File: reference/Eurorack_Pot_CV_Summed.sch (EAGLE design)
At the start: 10 parts, among them J1 Eurorack Jack, U1 MCP6004, U2 LM4040-10V

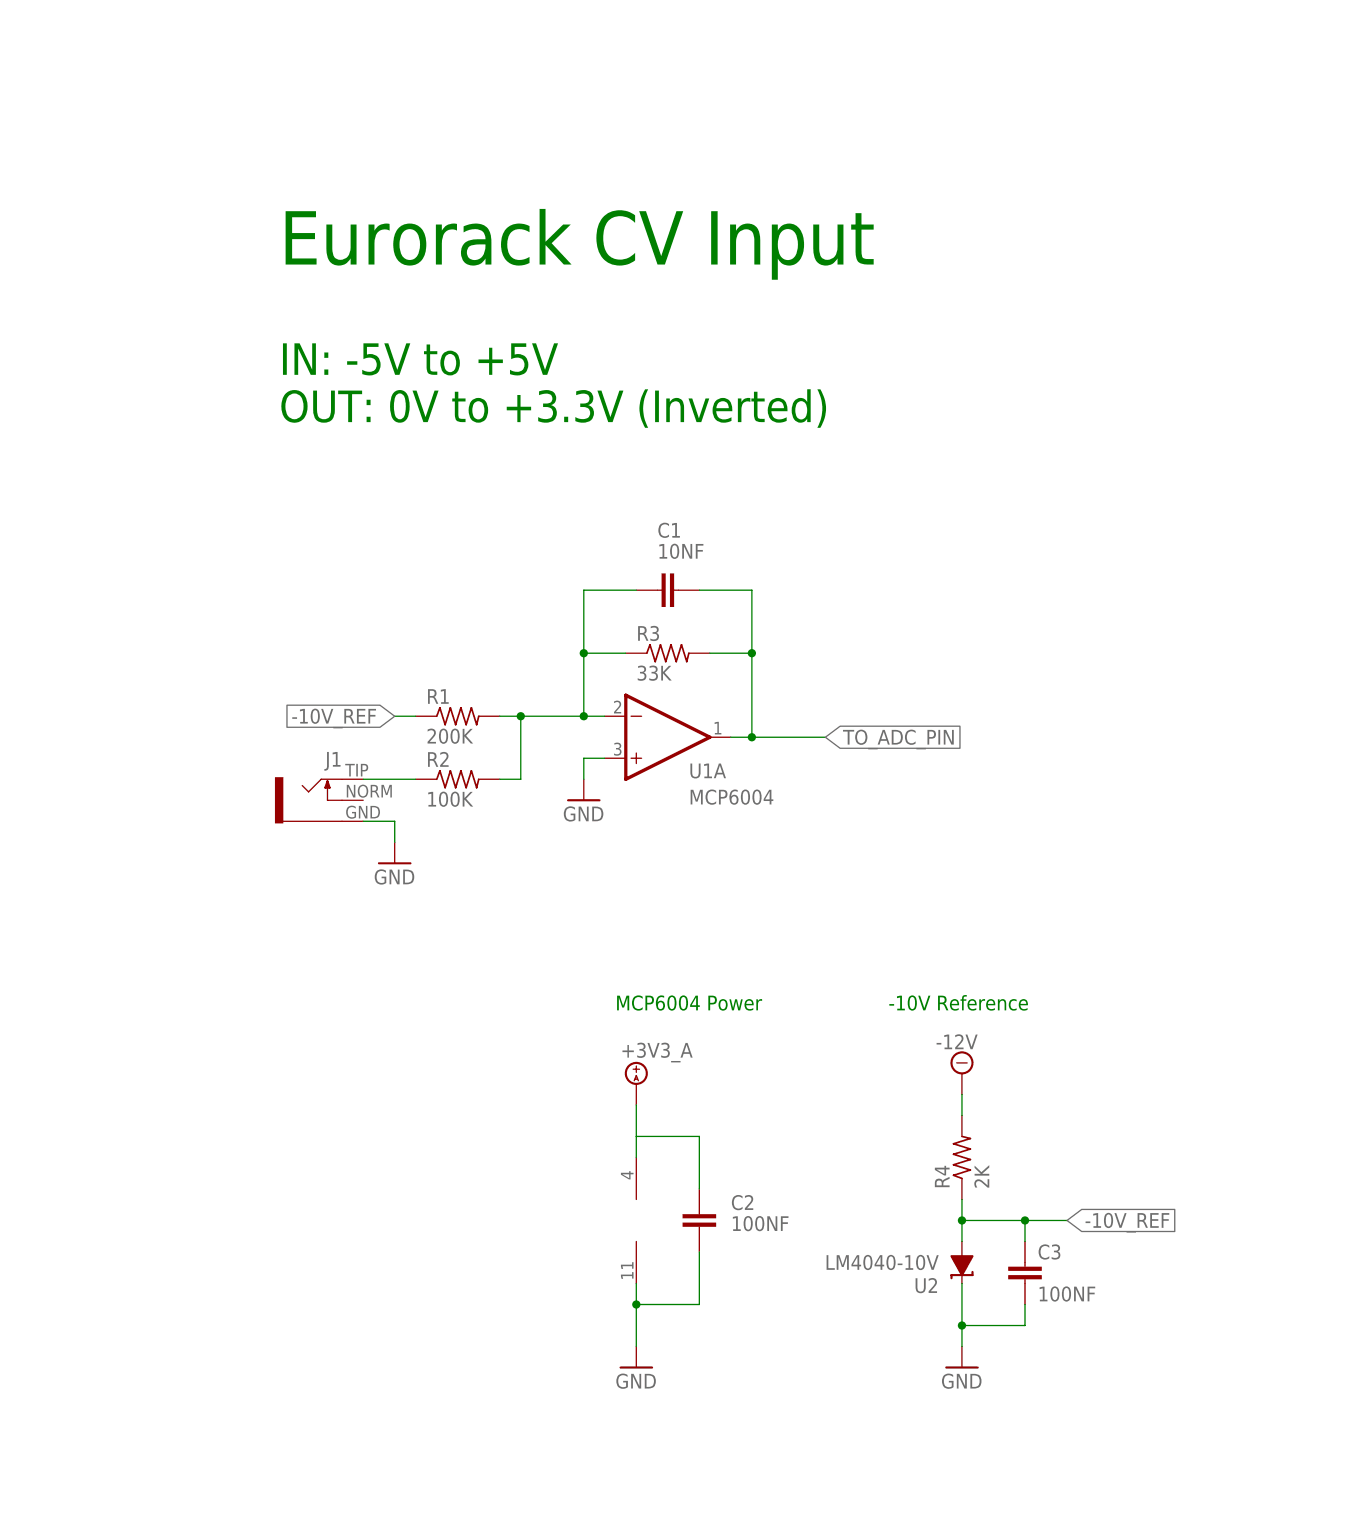
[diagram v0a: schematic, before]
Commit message: added pot in and pot cv summed
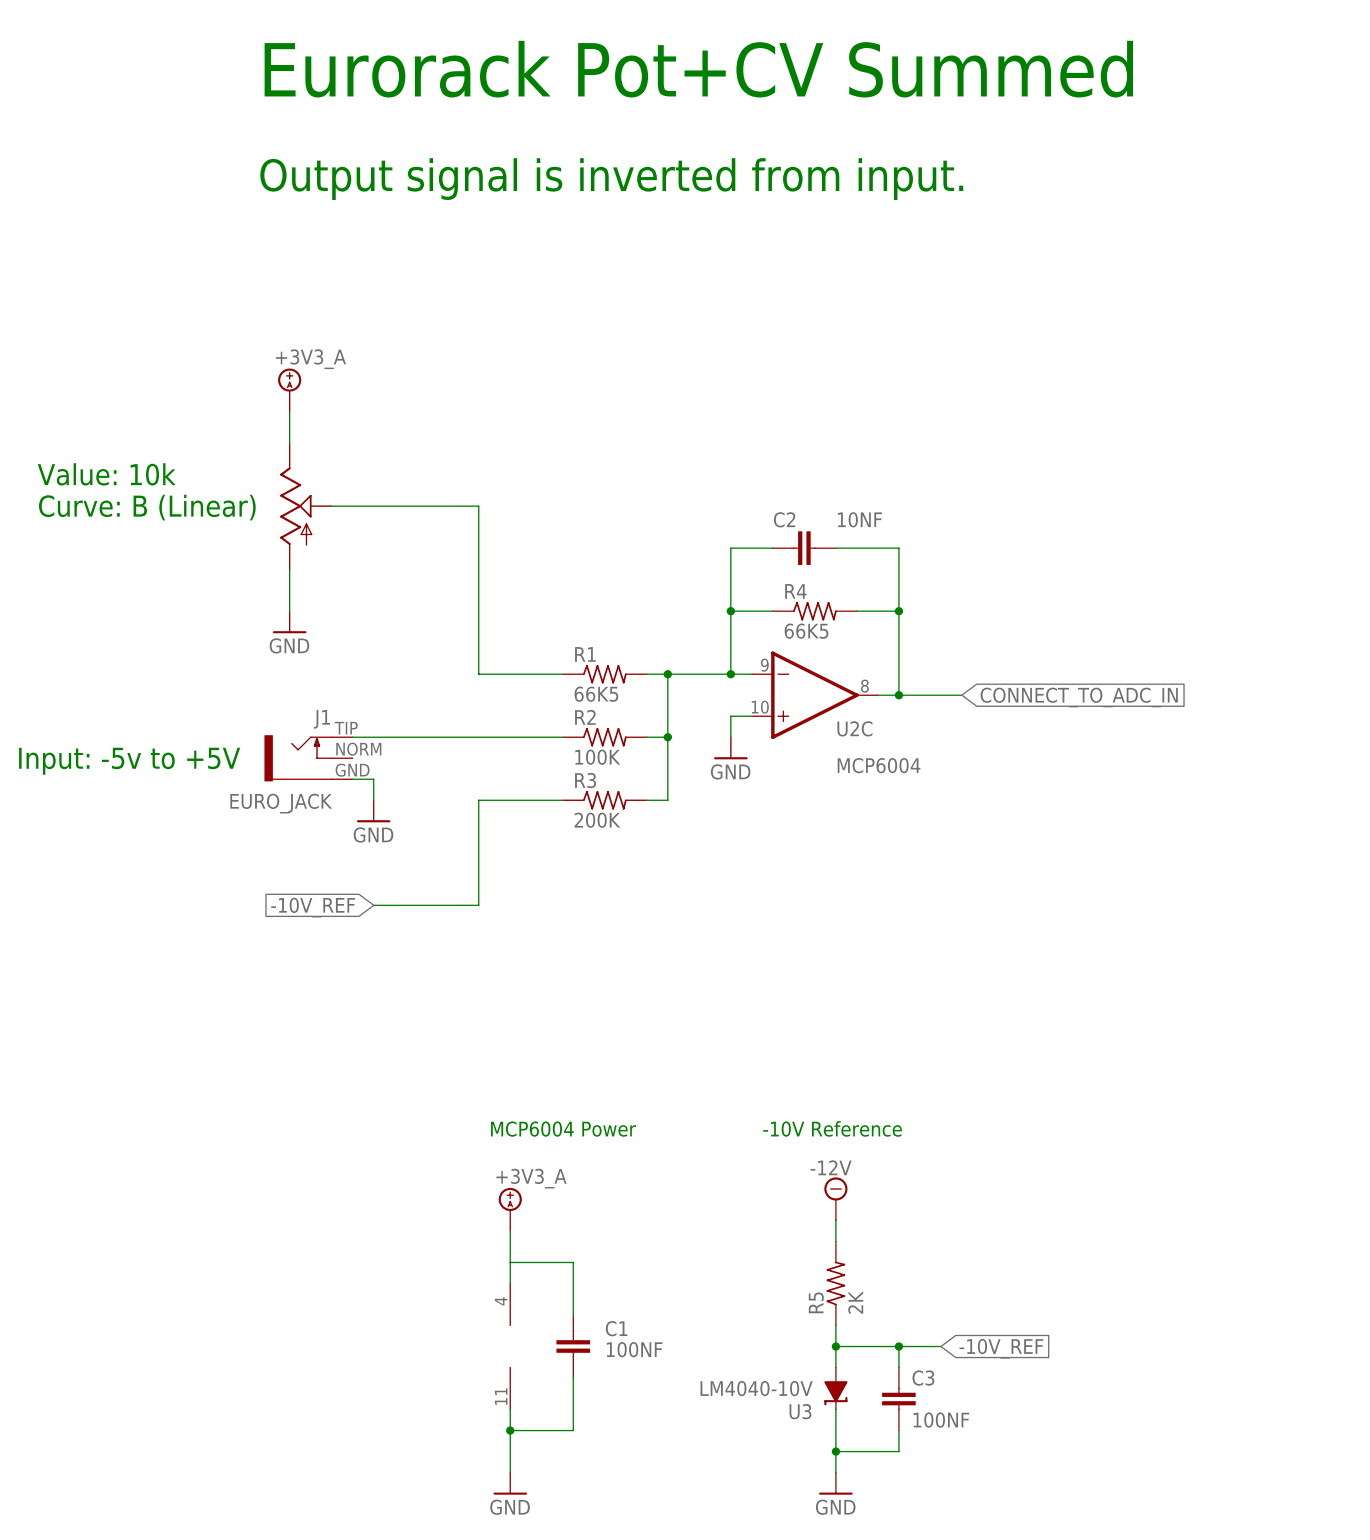
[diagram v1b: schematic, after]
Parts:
- added R5: 2K, Electrosmith-Passives:R-US_R0603
- added U3: LM4040-10V, Electrosmith-Power:LM4040-10VA12DBZ
- added VR1: (no value), Electrosmith-Interface:POT_9MM_SNAP-IN__
- C1: value 10NF -> 100NF
- C2: value 100NF -> 10NF
- J1: value Eurorack Jack -> EURO_JACK
- R1: value 200K -> 66K5
- R3: value 33K -> 200K
- R4: value 2K -> 66K5
- U2: value LM4040-10V -> MCP6004; device Electrosmith-Power:LM4040-10VA12DBZ -> Electrosmith-IC:MCP6004_TSSOP-14
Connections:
- net N$1 renamed CV_IN_1
- removed net N$3: C1.1, R1.2, R2.2, R3.1, U1A.-IN
- removed net TO_ADC_PIN: C1.2, R3.2, U1A.OUT
- new net CONNECT_TO_ADC_IN: C2.2, R4.2, U2C.OUT
- new net N$13: C2.1, R1.2, R2.2, R3.2, R4.1, U2C.-IN
- new net N$2: R1.1, VR1.2
- net +3V3_A: now also C1.2, VR1.3; no longer C2.2
- net -10V_REF: now also R3.1, R5.1, U3.A; no longer R1.1, R4.1, U2.A
- net -12V: now also R5.2; no longer R4.2
- net GND: now also C1.1, U2C.+IN, U3.C, VR1.1; no longer C2.1, U1A.+IN, U2.C
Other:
- note added: "Eurorack Pot+CV Summed"
- note added: "Input: -5v to +5V"
- note added: "Output signal is inverted from input."
- note added: "Value: 10k Curve: B (Linear)"
- note removed: "Eurorack CV Input"
- note removed: "IN: -5V to +5V OUT: 0V to +3.3V (Inverted)"
- moved on the sheet: C1, C2, C3, J1, R1, R2, R3, R4
